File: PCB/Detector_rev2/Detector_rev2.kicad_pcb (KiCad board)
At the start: 2 copper layers, 51.4 x 44.4 mm, 56 parts, among them J1 Conn_01x03_Male, J2 Conn_01x03_Male, J3 Conn_Coaxial, U1 N-jfet_dual, U2 N-jfet_dual, U3 LM6171D, U4 LM6171D, U5 LT6657BHMS8-5, U6 LT1995, U7 DMMT3904

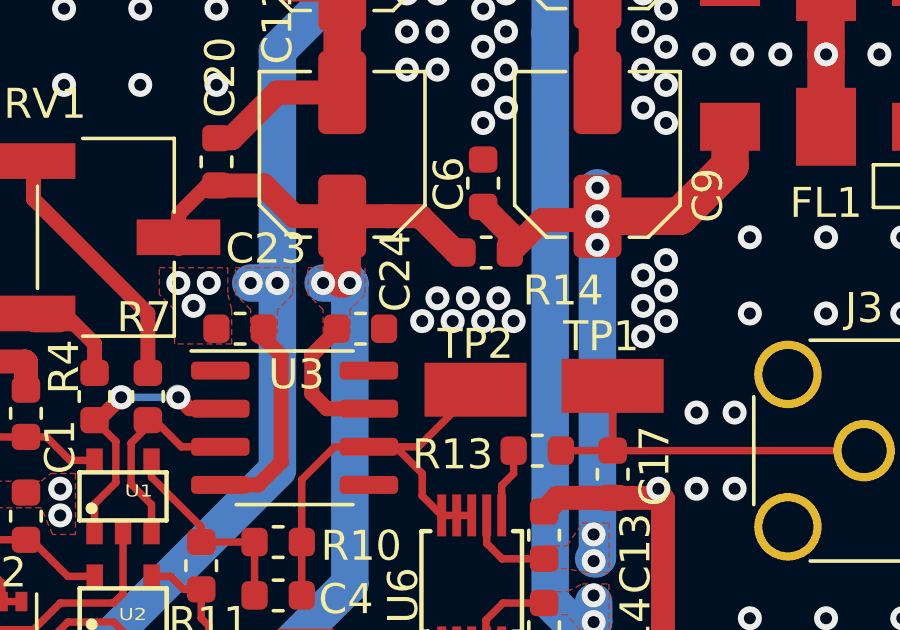
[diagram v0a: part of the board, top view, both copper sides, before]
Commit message: input terminal adjust
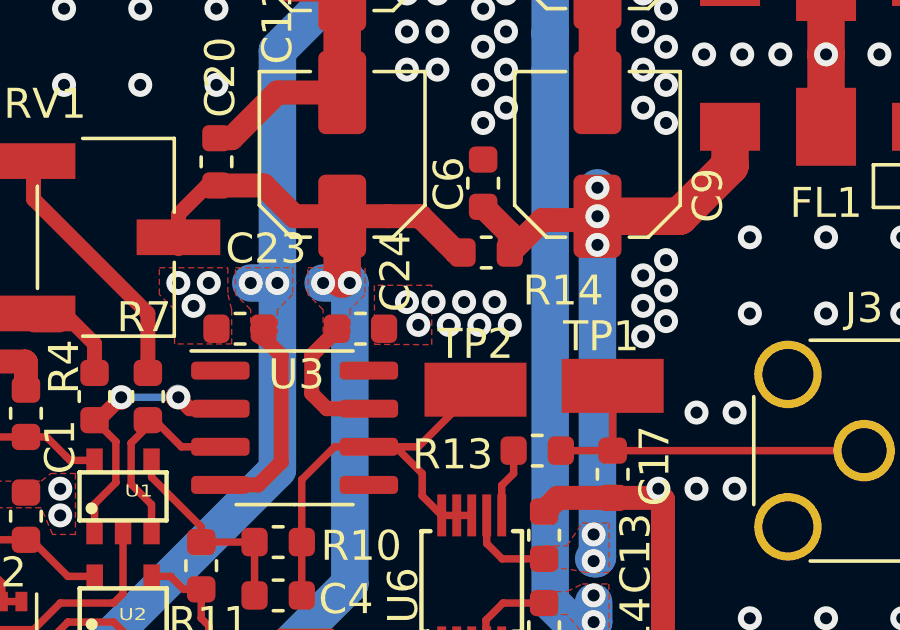
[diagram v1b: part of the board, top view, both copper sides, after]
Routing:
- net GND: vias 214 -> 215
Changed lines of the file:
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@@
-(kicad_pcb (version 20171130) (host pcbnew "(5.1.5)-3")
+(kicad_pcb (version 20171130) (host pcbnew "(5.1.0-0)")
   (general
     (thickness 1.6)
     (drawings 4)
-    (tracks 540)
+    (tracks 541)
     (zones 0)
     (modules 56)
@@
     (user_trace_width 1.25)
     (trace_clearance 0.2)
-    (zone_clearance 0.6)
+    (zone_clearance 0.2)
     (zone_45_only no)
     (trace_min 0.2)
@@
   (via (at 82.296 54.61) (size 0.8) (drill 0.4) (layers F.Cu B.Cu) (net 1))
   (via (at 82.296 55.88) (size 0.8) (drill 0.4) (layers F.Cu B.Cu) (net 1))
-  (via (at 74.676 61.722) (size 0.8) (drill 0.4) (layers F.Cu B.Cu) (net 1))
-  (via (at 75.692 61.722) (size 0.8) (drill 0.4) (layers F.Cu B.Cu) (net 1))
-  (via (at 76.708 61.722) (size 0.8) (drill 0.4) (layers F.Cu B.Cu) (net 1))
-  (via (at 74.168 62.484) (size 0.8) (drill 0.4) (layers F.Cu B.Cu) (net 1))
-  (via (at 75.184 62.484) (size 0.8) (drill 0.4) (layers F.Cu B.Cu) (net 1))
-  (via (at 76.2 62.484) (size 0.8) (drill 0.4) (layers F.Cu B.Cu) (net 1))
-  (via (at 77.216 62.484) (size 0.8) (drill 0.4) (layers F.Cu B.Cu) (net 1))
+  (via (at 74.549 61.849) (size 0.8) (drill 0.4) (layers F.Cu B.Cu) (net 1))
+  (via (at 75.565 61.849) (size 0.8) (drill 0.4) (layers F.Cu B.Cu) (net 1))
+  (via (at 76.581 61.849) (size 0.8) (drill 0.4) (layers F.Cu B.Cu) (net 1))
+  (via (at 74.041 62.611) (size 0.8) (drill 0.4) (layers F.Cu B.Cu) (net 1))
+  (via (at 75.057 62.611) (size 0.8) (drill 0.4) (layers F.Cu B.Cu) (net 1))
+  (via (at 76.073 62.611) (size 0.8) (drill 0.4) (layers F.Cu B.Cu) (net 1))
+  (via (at 77.089 62.611) (size 0.8) (drill 0.4) (layers F.Cu B.Cu) (net 1))
   (via (at 81.534 60.96) (size 0.8) (drill 0.4) (layers F.Cu B.Cu) (net 1))
   (via (at 81.534 61.976) (size 0.8) (drill 0.4) (layers F.Cu B.Cu) (net 1))
@@
   (via (at 74.93 44.45) (size 0.8) (drill 0.4) (layers F.Cu B.Cu) (net 1))
   (via (at 54.61 62.23) (size 0.8) (drill 0.4) (layers F.Cu B.Cu) (net 1))
+  (via (at 73.66 61.849) (size 0.8) (drill 0.4) (layers F.Cu B.Cu) (net 1))
   (segment (start 59.182 66.345) (end 60.96 66.345) (width 0.25) (layer F.Cu) (net 2))
   (segment (start 62.427 67.126) (end 63.246 67.126) (width 0.25) (layer F.Cu) (net 2))
@@
       (pts
         (xy 74.0156 59.8932) (xy 75.1332 61.0108) (xy 77.3176 61.0108) (xy 77.3176 61.2902) (xy 73.8124 61.2902)
-        (xy 73.8124 62.2046) (xy 73.533 62.2046) (xy 73.533 62.103) (xy 72.6694 62.103) (xy 72.6694 59.8678)
+        (xy 73.533 61.2902) (xy 72.6694 61.2902) (xy 72.6694 59.8678)
       )
     )
@@
       )
     )
+  )
+  (zone (net 1) (net_name GND) (layer F.Cu) (hatch edge 0.508)
+    (connect_pads yes (clearance 0.2))
+    (min_thickness 0.254)
+    (fill yes (arc_segments 32) (thermal_gap 0.508) (thermal_bridge_width 0.508))
+    (polygon
+      (pts
+        (xy 74.4855 61.2902) (xy 72.57415 61.2902) (xy 72.5805 63.2587) (xy 74.4855 63.2714)
+      )
+    )

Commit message: garberdata output
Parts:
- J2: footprint Connector_JST:JST_XH_S3B-XH-A-1_1x03_P2.50mm_Horizontal -> Detector_rev2:JST-XH_S3B
- moved J2 2.56 mm to (93.2, 53.6)
- moved J1 1.27 mm to (52.1, 68.3)
- moved H4 0.72 mm to (52.8, 45.7)
- moved H3 0.64 mm to (98.3, 84.5)
- moved TP2 0.51 mm to (75.5, 65.0)
- moved H2 0.51 mm to (98.3, 45.7)
- moved H1 0.35 mm to (52.8, 84.5)
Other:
- board size 51.4 x 44.4 mm -> 52.1 x 45.1 mm
- rule trace_min: 0.2 -> 0.01

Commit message: ADC driver pattern write
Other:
- rule solder_mask_min_width: 0.25 -> 0.001
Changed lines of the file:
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@@
     (pad_drill 0)
     (pad_to_mask_clearance 0.051)
-    (solder_mask_min_width 0.25)
+    (solder_mask_min_width 0.001)
     (aux_axis_origin 0 0)
     (visible_elements 7FFFFFFF)
     (pcbplotparams
       (layerselection 0x010fc_ffffffff)
-      (usegerberextensions false)
+      (usegerberextensions true)
       (usegerberattributes false)
       (usegerberadvancedattributes false)
@@
       (outputformat 1)
       (mirror false)
-      (drillshape 1)
+      (drillshape 0)
       (scaleselection 1)
       (outputdirectory ""))
